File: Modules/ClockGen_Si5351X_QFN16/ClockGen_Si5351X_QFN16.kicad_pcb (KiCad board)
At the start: 4 copper layers, 45.5 x 38.1 mm, 107 parts, among them J1 Screw Terminal, J10 2.54mm Stackable Socket, J11 2.54mm Stackable Socket, J12 2.54mm Stackable Socket, J13 2.54mm Stackable Socket, J14 2.54mm Stackable Socket, J2 JST SH, J3 SMA, J4 2.54 Pins, J5 2.54 Pins, J6 SMA, J7 SMA, J8 SMA, J9 SMA, Q1 GSFJ0300, Q2 GSFK0502, SW1 SW_SPDT, U1 NCV68261, U2 NCV68261, U3 NCP718BSNADJ, U4 SI5351B-B-GM1, U5 AP2127K-ADJ, Y1 25MHz

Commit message: PCB layout progress
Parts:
- moved H3 163.9 mm to (187.8, 118.1)
- moved H2 158.6 mm to (187.8, 86.1)
- moved H4 104.5 mm to (127.1, 118.1)
- moved C1 102.3 mm to (113.6, 123.9), turned to -90 degrees
- moved H1 100.0 mm to (127.1, 86.1)
- moved C5 44.4 mm to (148.9, 109.0), turned to -90 degrees
- moved D5 41.6 mm to (147.6, 105.1), turned to 90 degrees
- moved R4 41.0 mm to (147.4, 108.5)
- moved R5 40.7 mm to (147.4, 109.6), turned to 180 degrees
- moved D4 37.1 mm to (142.6, 99.3), turned to -90 degrees
- moved U5 34.8 mm to (152.1, 109.5)
- moved U2 31.5 mm to (144.3, 108.5)
- moved J5 30.5 mm to (136.9, 116.1)
- moved J4 30.5 mm to (180.6, 116.1)
- moved U3 26.9 mm to (144.3, 104.7)
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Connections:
- net Net-(J4-Pin_2) renamed +3V3
- C2 pad 1: Net-(J2-Pin_2) -> VCC
- J1 pad 2: VCC -> Net-(J1-Pin_2)
- J2 pad 2: Net-(J2-Pin_2) -> VCC
- Q1 pad 1: VCC -> Net-(J1-Pin_2)
- Q1 pad 6: Net-(J2-Pin_2) -> VCC
- RN1 pad 3: +3V0 -> /+5V_I2C_PULLUP
- RN1 pad 4: /+5V_I2C_PULLUP -> +3V0
- RN1 pad 5: /I2C_SCL_5V -> /I2C_SDA
- RN1 pad 6: /I2C_SCL -> /I2C_SDA_5V
- RN1 pad 7: /I2C_SDA -> /I2C_SCL
- RN1 pad 8: /I2C_SDA_5V -> /I2C_SCL_5V
- U2 pad 1: VCC -> Net-(J1-Pin_2)
- U2 pad 3: Net-(J2-Pin_2) -> VCC
- U2 pad 4: VCC -> Net-(J1-Pin_2)
- U2 pad 6: VCC -> Net-(J1-Pin_2)
- U3 pad 1: Net-(J2-Pin_2) -> VCC
- U3 pad 3: Net-(J2-Pin_2) -> VCC
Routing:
- net Net-(J1-Pin_2): track 0.00 -> 25.4 mm, vias 0 -> 1
- net GND: track 11.3 -> 24.2 mm, vias 12 -> 25
- net Net-(D4-A): track 0.00 -> 12.2 mm
- net VCC: track 0.00 -> 10.6 mm
- net /I2C_SDA: track 7.93 -> 18.5 mm, vias 0 -> 3
- net Net-(Q1A-G): track 0.00 -> 10.5 mm, vias 0 -> 2
- net /I2C_SCL_5V: track 0.00 -> 10.2 mm
- net +5V: track 0.00 -> 9.56 mm
- net Net-(JP1-C): track 0.00 -> 7.88 mm
- net /+5V_I2C_PULLUP: track 0.00 -> 7.78 mm
- net Net-(JP2-C): track 0.00 -> 7.25 mm
- net Net-(Q1B-G): track 0.00 -> 5.97 mm
- net /I2C_SDA_5V: track 0.00 -> 5.89 mm
- net +3V3: track 0.00 -> 5.45 mm
- net /I2C_SCL: track 7.88 -> 13.1 mm, vias 0 -> 2
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- added copper zone on In2.Cu, net +3V0
- added copper zone on B.Cu, net GND
- added copper zone on F.Cu, net GND
- added copper zone on In1.Cu, net GND
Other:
- board size 45.5 x 38.1 mm -> 66.8 x 38.1 mm
- board text added: "AB"
- board text added: "C"

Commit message: Most PCB layout done
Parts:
- C35, C36, C37, C38: footprint libraries:Worthington_C_0402 -> libraries:Worthington_C_0402_0603
- R2, R3: footprint libraries:Worthington_R_0201 -> libraries:Worthington_R_0402
- moved C38 134.9 mm to (175.8, 107.8)
- moved C34 133.0 mm to (172.5, 108.5), turned to -90 degrees
- moved C31 132.5 mm to (169.9, 108.5), turned to -90 degrees
- moved C22 132.1 mm to (164.6, 108.5), turned to -90 degrees
- moved L2 131.8 mm to (163.3, 108.5), turned to 90 degrees
- moved C30 131.5 mm to (163.4, 119.3)
- moved C33 131.2 mm to (166.0, 119.3)
- moved C17 131.1 mm to (161.9, 108.5), turned to -90 degrees
- moved C27 131.0 mm to (167.2, 108.5), turned to -90 degrees
- moved C25 130.2 mm to (160.8, 119.3)
- moved L7 130.1 mm to (165.9, 108.5), turned to 90 degrees
- moved L16 129.9 mm to (173.8, 108.5), turned to 90 degrees
- moved C20 129.3 mm to (158.8, 118.5), turned to -90 degrees
- moved C18 129.2 mm to (157.5, 117.0), turned to 90 degrees
- moved D6 128.6 mm to (154.9, 153.7)
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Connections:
- net /CLK0_BANDPASS renamed /CLK0_HIGHPASS
- net /CLK3_HIGHPASS renamed /CLK3_BANDPASS
- C17 pad 1: /CLK0 -> /CLK3
- C20 pad 1: /CLK3 -> /CLK0
- C22 pad 1: /CLK0 -> /CLK3
- C35 pad 1: Net-(C34-Pad1) -> Net-(C33-Pad2)
- C38 pad 1: Net-(C33-Pad2) -> Net-(C34-Pad1)
- L2 pad 2: /CLK0 -> /CLK3
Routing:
- net +5V: track 9.56 -> 63.2 mm, vias 0 -> 11
- net /~{OUTPUT_EN}: track 2.04 -> 24.3 mm, vias 0 -> 1
- net VCC: track 10.6 -> 32.1 mm
- net /CLK1: track 0.00 -> 17.8 mm
- net GND: track 24.2 -> 40.7 mm, vias 25 -> 73
- net +3V0: track 18.5 -> 34.8 mm, vias 7 -> 20
- net /CLK0: track 0.00 -> 15.6 mm
- net Net-(JP1-A): track 2.04 -> 17.4 mm, vias 0 -> 2
- net /CLK3: track 0.00 -> 11.4 mm
- net /CLK3_BANDPASS: track 12.0 -> 21.0 mm
- net /CLK2_BANDSTOP: track 11.8 -> 19.6 mm
- net /VCXO_IN/CLK_IN: track 12.0 -> 19.3 mm
- net /CLK2: track 0.00 -> 5.18 mm
- net Net-(C21-Pad2): track 0.00 -> 5.03 mm
- net Net-(C27-Pad1): track 0.00 -> 3.96 mm
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- added copper zone on F.Cu, net VCC
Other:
- outline, holes or cut-outs redrawn

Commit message: Schematic and PCB progress
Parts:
- added D11: RED, libraries:Worthington_LED_0402, F.Cu at (130.6, 128.1)
- added D12: 1N5819W, Diode_SMD:D_SOD-123F, F.Cu at (142.1, 102.1)
- added R13: 1k3, libraries:Worthington_R_0201, F.Cu at (130.2, 130.1)
- added S1: Breadboard 3D Model, libraries:Breadboard_400, F.Cu at (171.4, 140.2)
- C5: value 1u -> 10u
- R4: value 1k -> 200k
- R5: value 5k83 -> 49k9
- U3: value NCP718BSNADJ -> TPS7E8201
- moved J4 30.5 mm to (180.6, 85.6)
- moved D4 0.38 mm to (142.6, 98.9)
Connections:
- C1 pad 1: +5V -> VCC
- C2 pad 1: VCC -> Net-(D12-K)
- D4 pad 2: Net-(D4-A) -> VCC
- D5 pad 2: Net-(D4-A) -> VCC
- J1 pad 1: GND -> /PWR_IN
- J1 pad 2: Net-(J1-Pin_2) -> GND
- J2 pad 2: VCC -> Net-(D12-K)
- J4 pad 1: GND -> unconnected-(J4-Pin_1-Pad1)
- J4 pad 2: +3V3 -> unconnected-(J4-Pin_2-Pad2)
- J4 pad 3: GND -> unconnected-(J4-Pin_3-Pad3)
- J4 pad 4: +3V3 -> unconnected-(J4-Pin_4-Pad4)
- J5 pad 2: +5V -> Net-(D11-K)
- J5 pad 4: +5V -> Net-(D11-K)
- Q1 pad 1: Net-(J1-Pin_2) -> /PWR_IN
- Q1 pad 3: +5V -> VCC
- Q1 pad 4: +3V3 -> Net-(D11-K)
- Q1 pad 6: VCC -> Net-(D12-K)
- R4 pad 2: Net-(D4-A) -> VCC
- U1 pad 1: +3V3 -> Net-(D11-K)
- U1 pad 3: +5V -> VCC
- U1 pad 4: +3V3 -> Net-(D11-K)
- U1 pad 6: +3V3 -> Net-(D11-K)
- U2 pad 1: Net-(J1-Pin_2) -> /PWR_IN
- U2 pad 3: VCC -> Net-(D12-K)
- U2 pad 4: Net-(J1-Pin_2) -> /PWR_IN
- U2 pad 6: Net-(J1-Pin_2) -> /PWR_IN
- U3 pad 1: VCC -> Net-(D12-K)
- U3 pad 3: VCC -> Net-(D12-K)
- U3 pad 5: Net-(D4-A) -> VCC
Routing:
- net +5V: track 63.2 -> 0.00 mm, vias 11 -> 0
- net Net-(D11-K): track 0.00 -> 55.6 mm
- net VCC: track 32.1 -> 75.7 mm, vias 0 -> 11
- net /PWR_IN: track 0.00 -> 33.1 mm, vias 0 -> 2
- net Net-(D12-K): track 0.00 -> 32.1 mm
- net Net-(J1-Pin_2): track 24.3 -> 0.00 mm, vias 1 -> 0
- net Net-(D4-A): track 13.0 -> 0.00 mm
- net +3V3: track 8.92 -> 0.00 mm
- net GND: track 40.7 -> 41.0 mm, vias 73 -> 86
- added copper zone on F.Cu, net /PWR_IN
- added copper zone on F.Cu, net Net-(D12-K)
- removed copper zone on F.Cu, net VCC

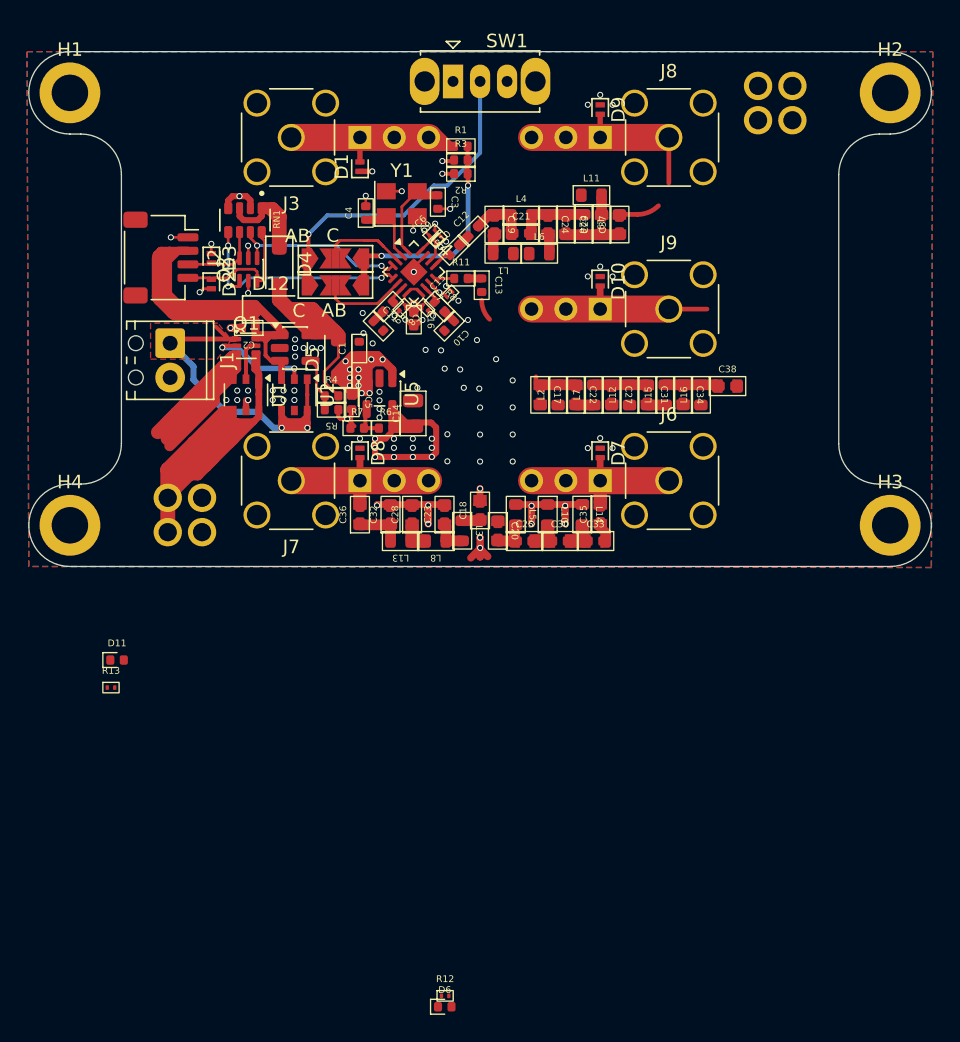
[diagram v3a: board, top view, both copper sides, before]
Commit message: PCB Layout finished
Need to tweak silkscreen and add art and stuff
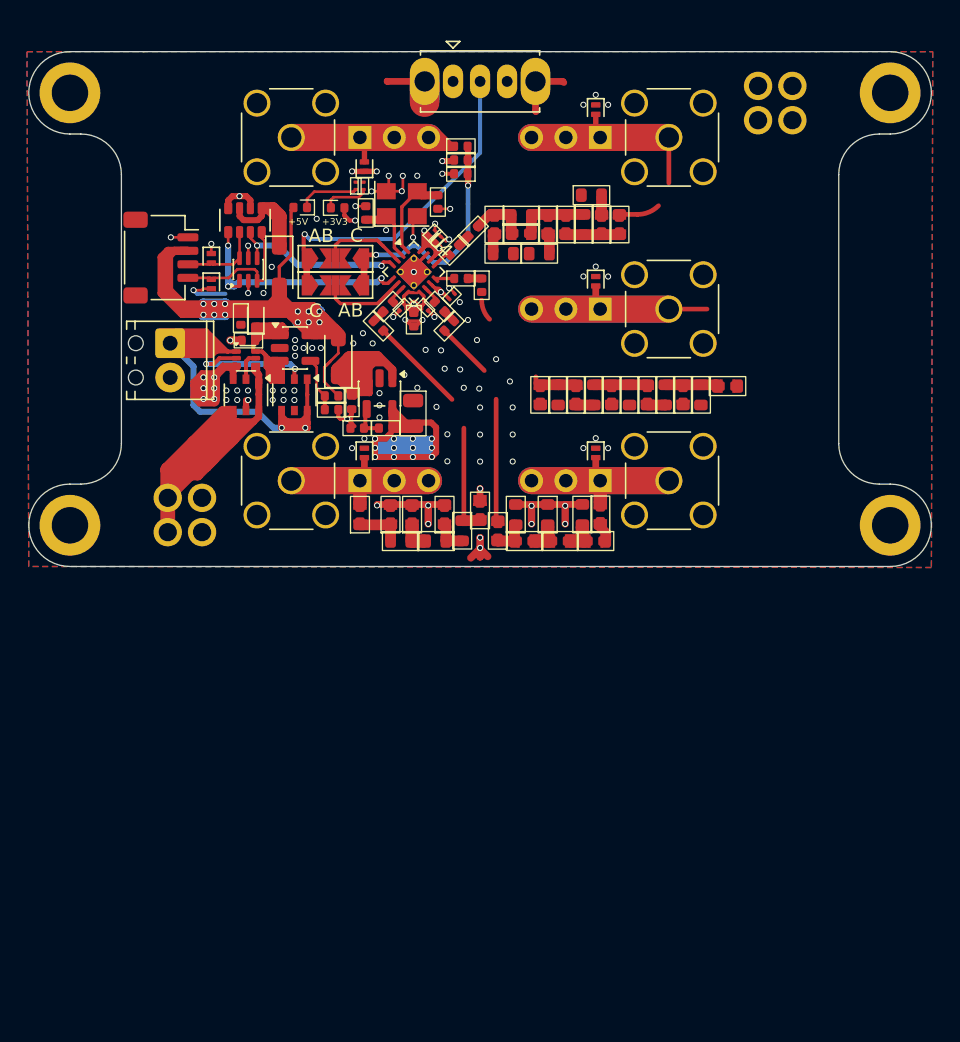
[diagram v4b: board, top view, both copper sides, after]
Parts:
- D12: value 1N5819W -> RB521S-30; footprint Diode_SMD:D_SOD-123F -> Diode_SMD:D_SOD-523
- R12, R13: value 1k3 -> 1k8
- U4: footprint Package_DFN_QFN:QFN-16-1EP_3x3mm_P0.5mm_EP1.45x1.45mm -> Package_DFN_QFN:QFN-16-1EP_3x3mm_P0.5mm_EP1.9x1.9mm_ThermalVias
- moved R12 60.2 mm to (148.8, 93.0), turned to 90 degrees
- moved D6 59.7 mm to (146.9, 94.6)
- moved R13 41.3 mm to (148.3, 93.0), turned to 90 degrees
- moved D11 36.1 mm to (144.2, 94.6), turned to 180 degrees
- moved C1 9.05 mm to (139.8, 102.8), turned to -90 degrees
- moved D12 1.35 mm to (140.9, 102.7), turned to 90 degrees
- moved C2 0.92 mm to (140.3, 104.4)
- moved Q1 0.92 mm to (140.2, 105.7)
- moved D1 0.33 mm to (148.9, 91.6)
- moved D10 0.33 mm to (166.0, 100.1)
- moved D7 0.33 mm to (166.0, 112.8)
- moved D8 0.33 mm to (148.9, 112.8)
- moved D9 0.33 mm to (166.0, 87.3)
- moved C15 0.23 mm to (155.4, 101.2)
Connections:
- net +3V0 renamed +3V3
- D11 pad 2: Net-(D11-A) -> VCC
- J2 pad 2: Net-(D12-K) -> VCC
- J5 pad 2: Net-(D11-K) -> Net-(J5-Pin_2)
- J5 pad 4: Net-(D11-K) -> Net-(J5-Pin_2)
- Q1 pad 4: Net-(D11-K) -> Net-(J5-Pin_2)
- R13 pad 1: Net-(D11-A) -> Net-(D11-K)
- U1 pad 1: Net-(D11-K) -> Net-(J5-Pin_2)
- U1 pad 4: Net-(D11-K) -> Net-(J5-Pin_2)
- U1 pad 6: Net-(D11-K) -> Net-(J5-Pin_2)
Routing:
- net +3V3: track 34.8 -> 88.1 mm, vias 20 -> 21
- net Net-(D11-K): track 55.6 -> 4.53 mm
- net Net-(J5-Pin_2): track 0.00 -> 49.8 mm
- net VCC: track 75.7 -> 107.1 mm, vias 11 -> 18
- net GND: track 41.0 -> 68.1 mm, vias 86 -> 95
- net +5V: track 0.00 -> 27.0 mm
- net /PWR_IN: track 33.1 -> 46.5 mm
- net Net-(D12-K): track 32.1 -> 20.5 mm
- net /CLK1_LOWPASS: track 13.3 -> 23.4 mm
- net /VCXO_IN/CLK_IN: track 19.3 -> 29.5 mm
- net /CLK3_BANDPASS: track 21.0 -> 31.2 mm
- net /CLK2_BANDSTOP: track 19.6 -> 29.7 mm
- net /CLK0_HIGHPASS: track 12.7 -> 22.8 mm
- net Net-(D6-K): track 0.00 -> 3.45 mm
- net /I2C_SDA: track 17.6 -> 20.0 mm
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- added copper zone on In2.Cu, net VCC
- removed copper zone on F.Cu, net /PWR_IN
- removed copper zone on F.Cu, net Net-(D12-K)
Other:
- board text added: "+3V3"
- board text added: "+5V"

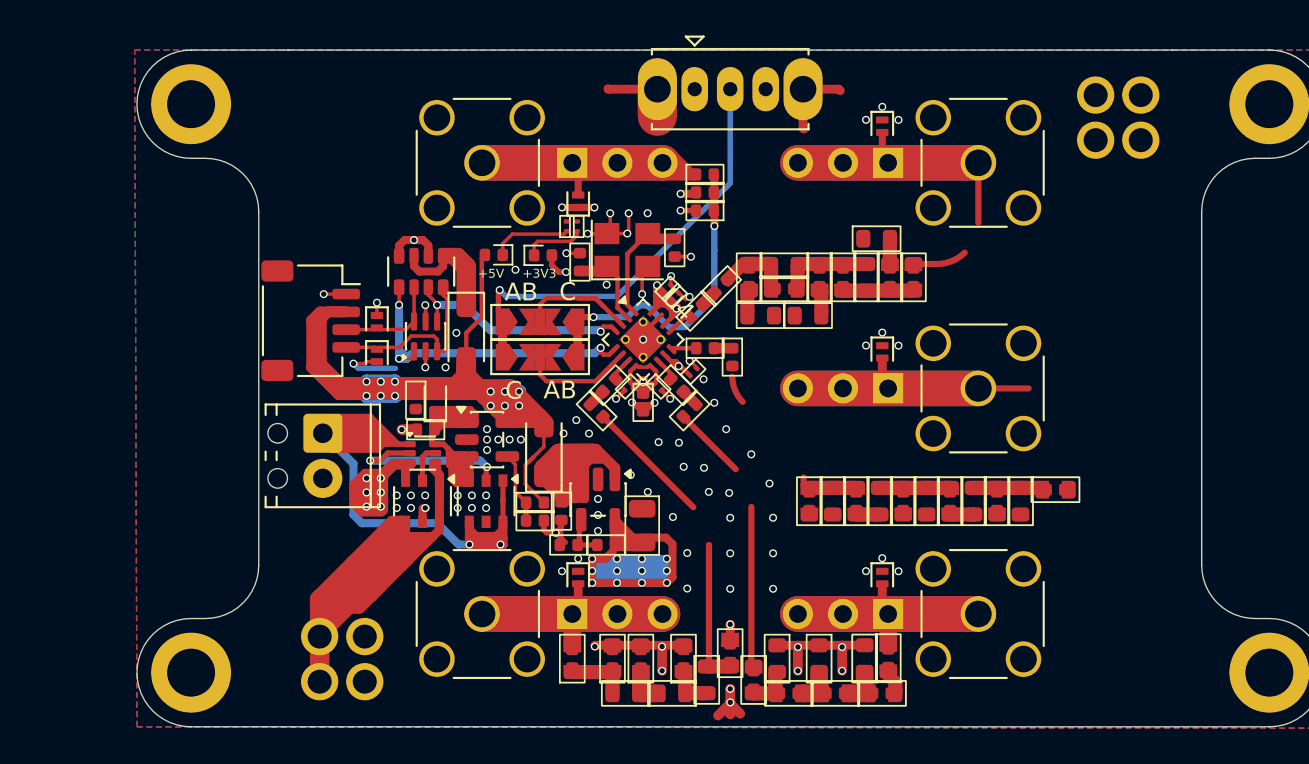
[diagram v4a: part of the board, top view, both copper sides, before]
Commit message: Modified designn to include LM66200
PCB layout edits in progress
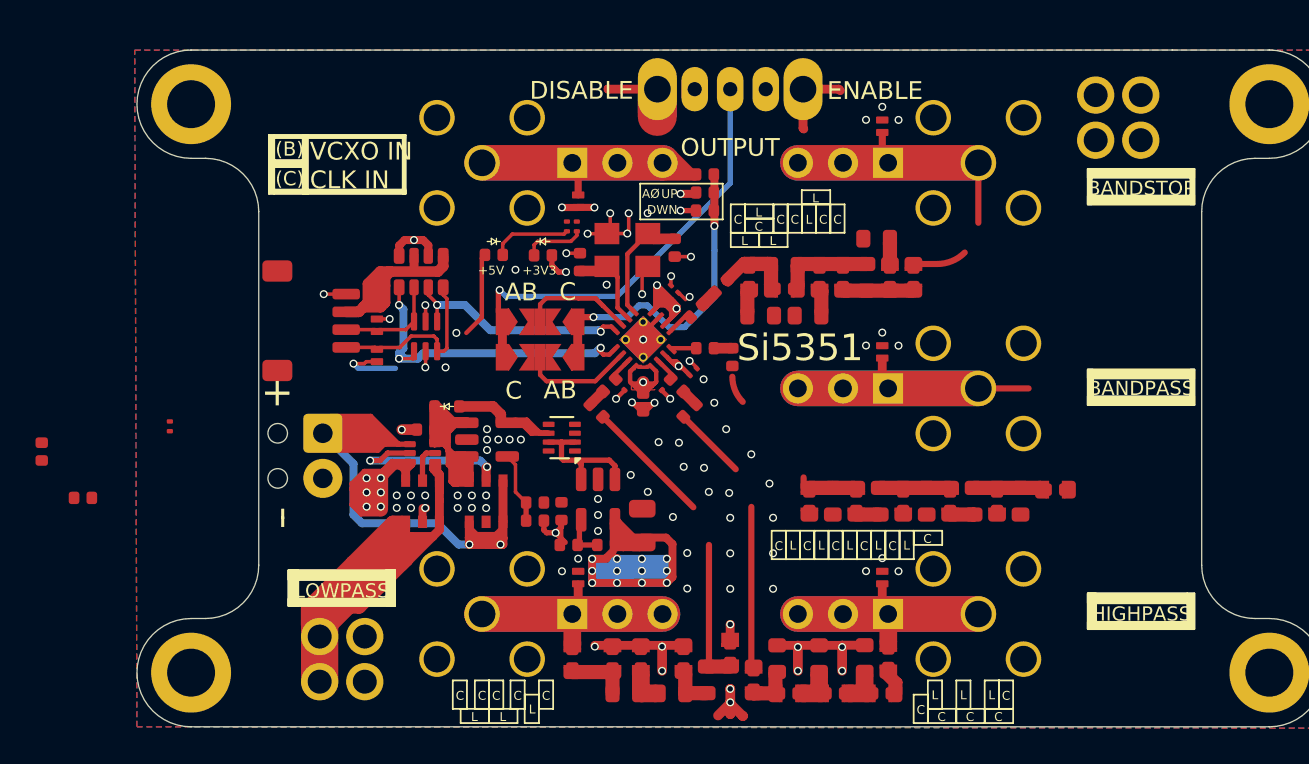
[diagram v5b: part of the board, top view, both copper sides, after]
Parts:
- removed D4, D5: 1N5819W, Diode_SMD:D_SOD-123F
- removed the S1 at (171.4, 140.2)
- added C39: 1u, libraries:Worthington_C_0402, F.Cu at (121.0, 108.3)
- added G***: LOGO, libraries:stemma_qt, B.Cu at (132.8, 98.3)
- added R14: 10k, libraries:Worthington_R_0201, F.Cu at (125.9, 104.2)
- added U6: LM66200, Package_TO_SOT_SMD:SOT-583-8, F.Cu at (148.0, 104.9)
- R4: value 200k -> 31k6
- R5: value 49k9 -> 10k
- moved C1 21.3 mm to (118.7, 105.7)
- moved D12 0.78 mm to (141.5, 103.1), turned to 0 degrees
- moved D3 0.20 mm to (137.6, 98.6)
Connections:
- net +5V renamed /V_REG
- C1 pad 1: VCC -> +5V_INT
- D11 pad 2: VCC -> +5V_INT
- D12 pad 2: VCC -> +5V_INT
- J2 pad 2: VCC -> /I2C_HIGHSIDE
- Q1 pad 3: VCC -> +5V_INT
- R4 pad 2: VCC -> +5V_INT
- RN1 pad 1: /+5V_I2C_PULLUP -> /I2C_HIGHSIDE
- RN1 pad 3: /+5V_I2C_PULLUP -> /I2C_HIGHSIDE
- U1 pad 3: VCC -> +5V_INT
- U3 pad 5: VCC -> +5V_INT
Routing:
- net VCC: track 107.1 -> 0.00 mm, vias 18 -> 0
- net +5V_INT: track 0.00 -> 44.5 mm, vias 0 -> 7
- net /V_REG: track 27.0 -> 7.51 mm
- net /I2C_HIGHSIDE: track 0.00 -> 14.9 mm
- net /+5V_I2C_PULLUP: track 7.44 -> 0.00 mm
- net Net-(J5-Pin_2): track 49.8 -> 52.0 mm
- net /I2C_SDA: track 20.0 -> 18.7 mm
- net Net-(Q1A-G): track 9.90 -> 10.7 mm
- net /PWR_IN: track 46.5 -> 47.2 mm
- net Net-(D12-K): track 20.5 -> 21.1 mm
- net GND: track 68.1 -> 68.3 mm, vias 95 -> 91
- added copper zone on In2.Cu, net +5V_INT
- removed copper zone on In2.Cu, net VCC
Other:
- board text added: "(B)"
- board text added: "(C)"
- board text added: "+"
- board text added: "-"
- board text added: "AØ"
- board text added: "BANDPASS"
- board text added: "BANDSTOP"
- board text added: "DISABLE"
- board text added: "DWN"
- board text added: "ENABLE"
- board text added: "HIGHPASS"
- board text added: "L"
- board text added: "LOWPASS"
- board text added: "OUTPUT"
- board text added: "Si5351"
- board text added: "UP"
- board text added: "VCXO IN CLK IN"

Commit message: PCB Layout
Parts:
- R4, R5, R6, R7: footprint libraries:Worthington_R_0402 -> libraries:Worthington_R_0201
- U1, U2: value NCV68261 -> NCV68061
- moved C39 25.3 mm to (146.2, 104.9), turned to -90 degrees
- moved R14 20.4 mm to (146.2, 106.3), turned to -90 degrees
- moved C1 18.6 mm to (136.8, 110.0), turned to -135 degrees
- moved R5 9.26 mm to (140.7, 102.3), turned to 0 degrees
- moved R4 7.78 mm to (141.8, 102.3)
- moved U5 2.72 mm to (147.3, 108.5)
- moved C5 2.66 mm to (149.6, 106.9), turned to 90 degrees
- moved R6 1.98 mm to (148.5, 110.8)
- moved C14 1.14 mm to (151.8, 109.0), turned to -45 degrees
- moved R7 0.81 mm to (147.6, 111.1), turned to 90 degrees
- moved R3 0.39 mm to (156.1, 91.5)
- moved R2 0.39 mm to (156.1, 92.5)
- moved R1 0.15 mm to (156.1, 89.9)
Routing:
- net /I2C_HIGHSIDE: track 14.9 -> 79.5 mm
- net +5V_INT: track 44.5 -> 68.0 mm, vias 7 -> 12
- net GND: track 68.3 -> 84.0 mm, vias 91 -> 166
- net /VCXO_IN/CLK_IN: track 29.5 -> 17.5 mm
- net /V_REG: track 7.51 -> 19.0 mm
- net /CLK1_LOWPASS: track 23.4 -> 13.3 mm
- net /CLK3_BANDPASS: track 31.2 -> 21.0 mm
- net /CLK0_HIGHPASS: track 22.8 -> 12.7 mm
- net /CLK2_BANDSTOP: track 29.7 -> 19.6 mm
- net Net-(U3-ADJ): track 4.19 -> 9.13 mm, vias 0 -> 2
- net Net-(U6-ST): track 0.00 -> 1.17 mm
- net +3V3: vias 21 -> 18
